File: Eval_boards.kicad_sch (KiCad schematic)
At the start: 0 parts

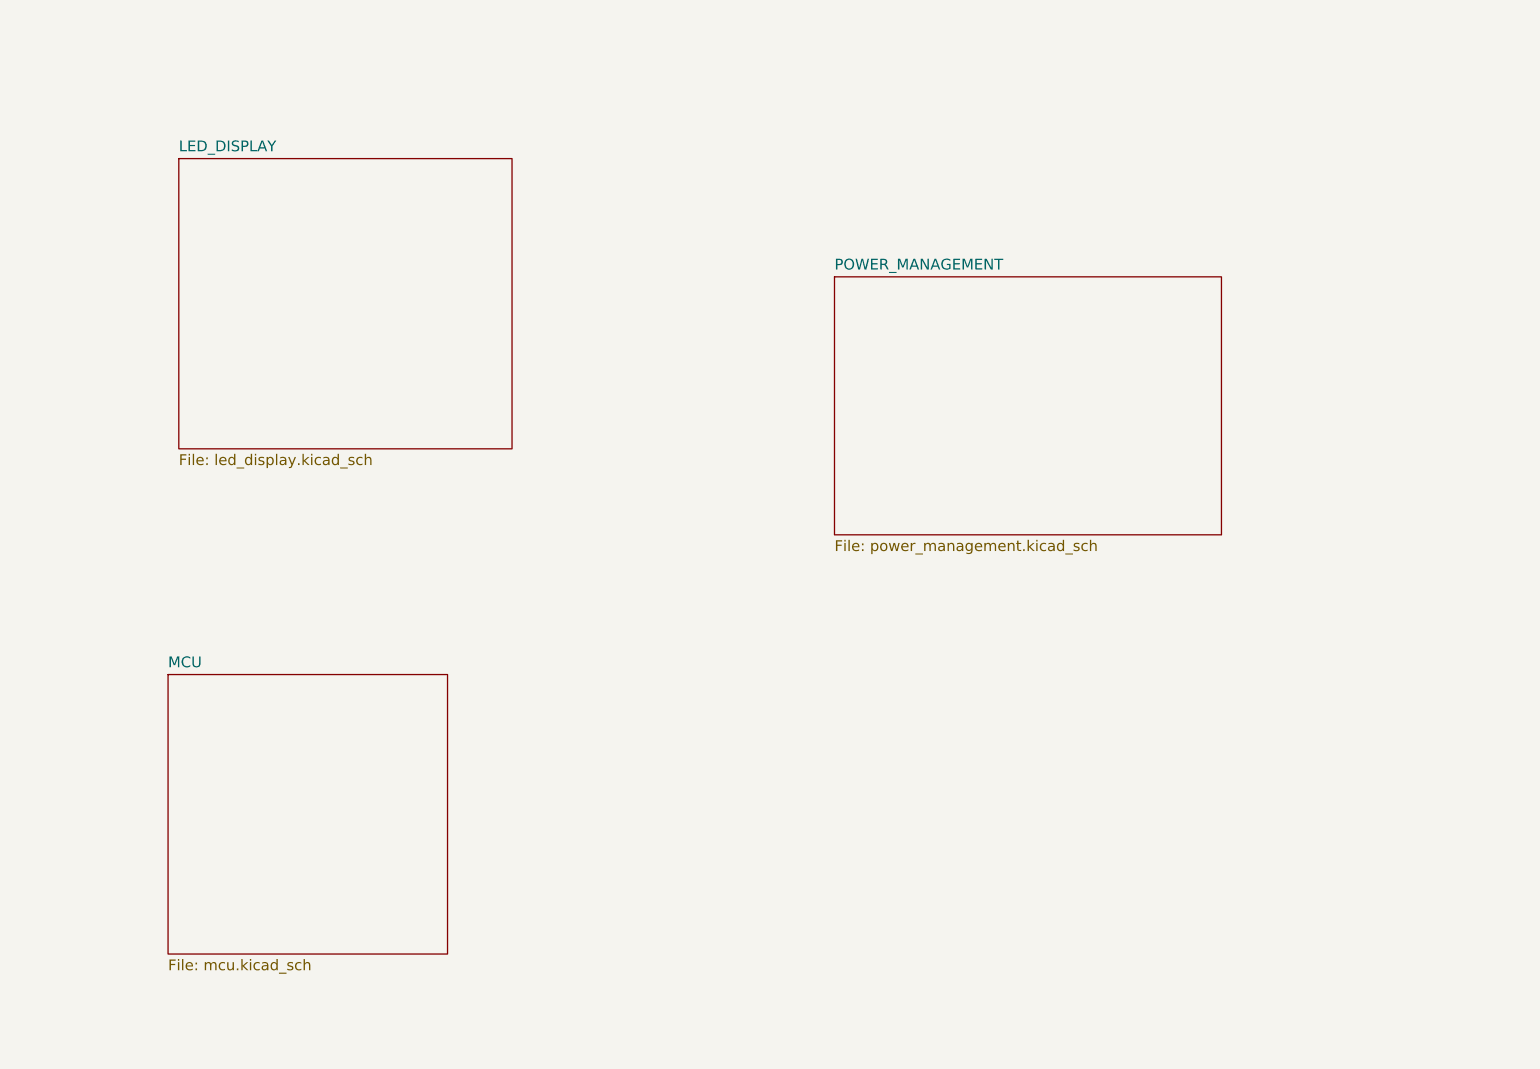
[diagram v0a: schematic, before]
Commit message: Change of concept - one board, not multiple
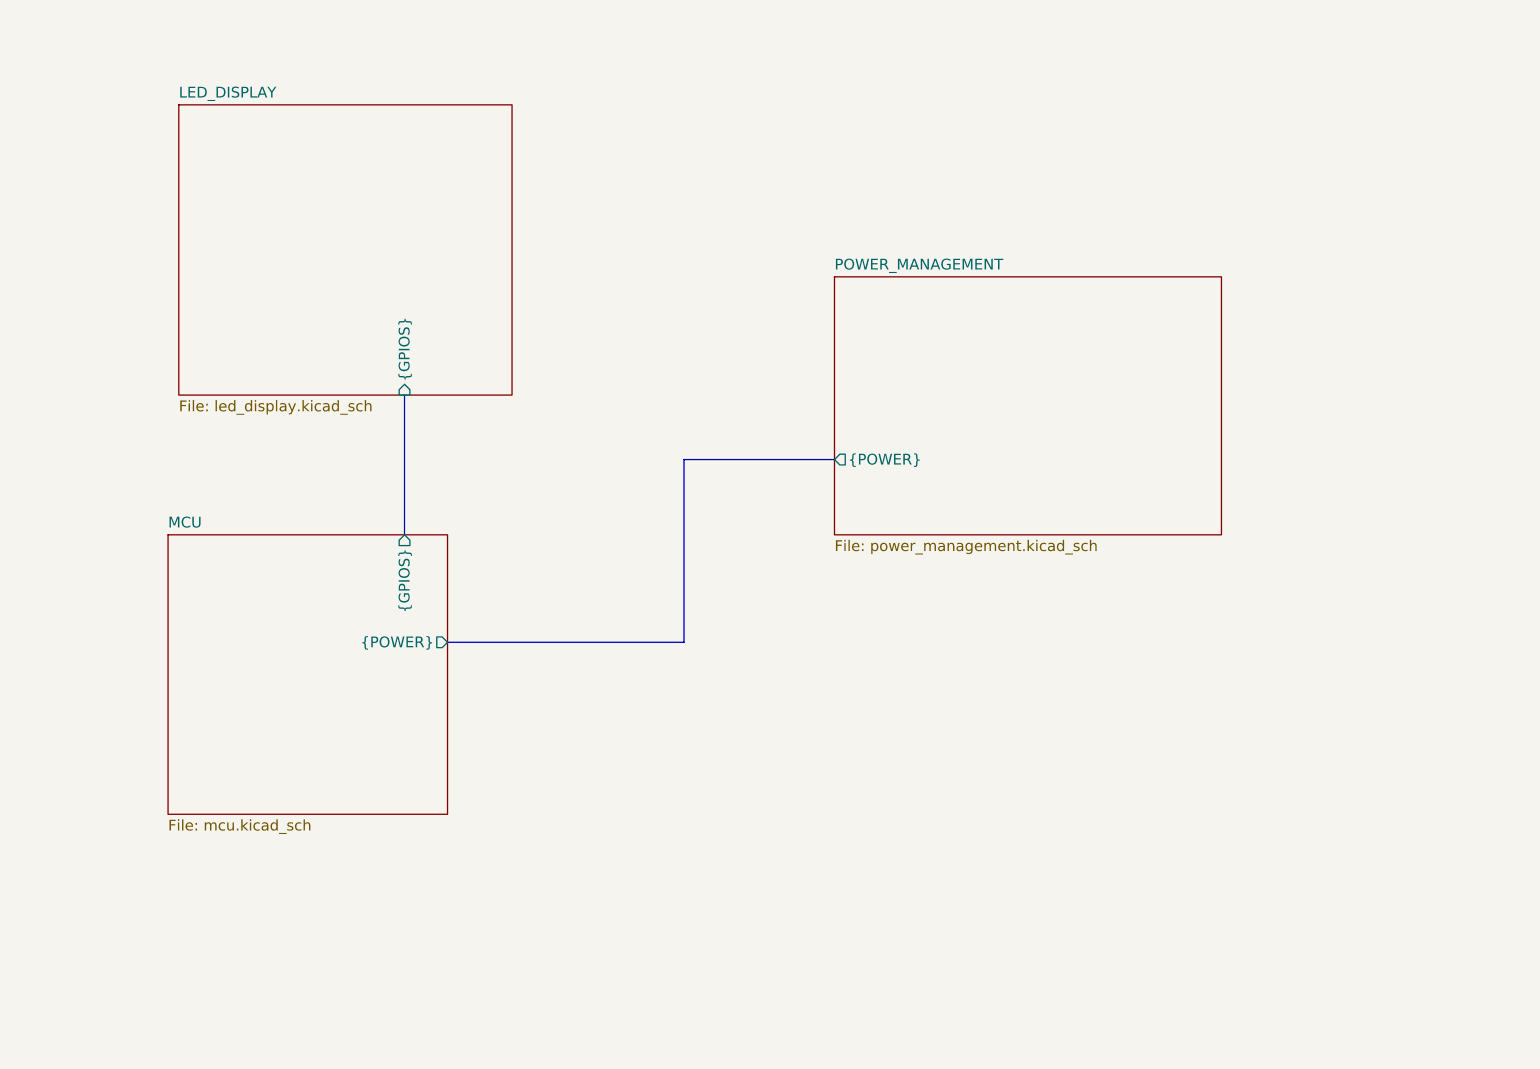
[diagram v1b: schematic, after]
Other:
- sheet LED_DISPLAY ports: added {GPIOS}; removed none
- sheet MCU ports: added {GPIOS}, {POWER}; removed none
- sheet POWER_MANAGEMENT ports: added {POWER}; removed none
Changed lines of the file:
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@@
 		(date "2025-09-10")
 	)
+	(bus
+		(pts
+			(xy 95.25 66.04) (xy 95.25 87.63)
+		)
+		(stroke
+			(width 0)
+			(type default)
+		)
+	)
+	(bus
+		(pts
+			(xy 62.23 58.42) (xy 62.23 74.93)
+		)
+		(stroke
+			(width 0)
+			(type default)
+		)
+	)
+	(bus
+		(pts
+			(xy 95.25 87.63) (xy 67.31 87.63)
+		)
+		(stroke
+			(width 0)
+			(type default)
+		)
+	)
+	(bus
+		(pts
+			(xy 113.03 66.04) (xy 95.25 66.04)
+		)
+		(stroke
+			(width 0)
+			(type default)
+		)
+	)
 	(sheet
-		(at 35.56 30.48)
+		(at 35.56 24.13)
 		(size 39.37 34.29)
 		(exclude_from_sim no)
@@
 		)
 		(property "Sheetname" "LED_DISPLAY"
-			(at 35.56 29.7684 0)
+			(at 35.56 23.4184 0)
 			(effects
 				(font
@@
 		)
 		(property "Sheetfile" "led_display.kicad_sch"
-			(at 35.56 65.3546 0)
+			(at 35.56 59.0046 0)
 			(effects
 				(font
@@
 				)
 				(justify left top)
+			)
+		)
+		(pin "{GPIOS}" input
+			(at 62.23 58.42 270)
+			(effects
+				(font
+					(size 1.27 1.27)
+				)
+				(justify left)
 			)
 		)
@@
 			)
 		)
+		(pin "{POWER}" output
+			(at 113.03 66.04 180)
+			(effects
+				(font
+					(size 1.27 1.27)
+				)
+				(justify left)
+			)
+		)
 		(instances
 			(project "Eval_boards"
@@
 	)
 	(sheet
-		(at 34.29 91.44)
+		(at 34.29 74.93)
 		(size 33.02 33.02)
 		(exclude_from_sim no)
@@
 		)
 		(property "Sheetname" "MCU"
-			(at 34.29 90.7284 0)
+			(at 34.29 74.2184 0)
 			(effects
 				(font
@@
 		)
 		(property "Sheetfile" "mcu.kicad_sch"
-			(at 34.29 125.0446 0)
+			(at 34.29 108.5346 0)
 			(effects
 				(font
@@
 			)
 		)
+		(pin "{GPIOS}" output
+			(at 62.23 74.93 90)
+			(effects
+				(font
+					(size 1.27 1.27)
+				)
+				(justify right)
+			)
+		)
+		(pin "{POWER}" output
+			(at 67.31 87.63 0)
+			(effects
+				(font
+					(size 1.27 1.27)
+				)
+				(justify right)
+			)
+		)

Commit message: Finished pcb project
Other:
- added sheet ACCELEROMETER (accelerometer.kicad_sch)
- sheet MCU ports: added {ACCELEROMETER}; removed none
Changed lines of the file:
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@@
 	(bus
 		(pts
-			(xy 95.25 66.04) (xy 95.25 87.63)
+			(xy 118.11 62.23) (xy 123.19 62.23)
 		)
 		(stroke
@@
 	(bus
 		(pts
-			(xy 62.23 58.42) (xy 62.23 74.93)
+			(xy 62.23 62.23) (xy 67.31 62.23)
 		)
 		(stroke
@@
 	(bus
 		(pts
-			(xy 95.25 87.63) (xy 67.31 87.63)
+			(xy 95.25 48.26) (xy 95.25 54.61)
 		)
 		(stroke
@@
 		)
 	)
-	(bus
-		(pts
-			(xy 113.03 66.04) (xy 95.25 66.04)
-		)
-		(stroke
-			(width 0)
-			(type default)
-		)
-	)
-	(sheet
-		(at 35.56 24.13)
-		(size 39.37 34.29)
+	(sheet
+		(at 123.19 16.51)
+		(size 71.12 83.82)
 		(exclude_from_sim no)
 		(in_bom yes)
@@
 		)
 		(property "Sheetname" "LED_DISPLAY"
-			(at 35.56 23.4184 0)
+			(at 123.19 15.7984 0)
 			(effects
 				(font
@@
 		)
 		(property "Sheetfile" "led_display.kicad_sch"
-			(at 35.56 59.0046 0)
+			(at 123.19 100.9146 0)
 			(effects
 				(font
@@
 		)
 		(pin "{GPIOS}" input
-			(at 62.23 58.42 270)
+			(at 123.19 62.23 180)
 			(effects
 				(font
@@
 	)
 	(sheet
-		(at 113.03 44.45)
-		(size 45.72 30.48)
+		(at 16.51 16.51)
+		(size 45.72 116.84)
 		(exclude_from_sim no)
 		(in_bom yes)
@@
 		)
 		(property "Sheetname" "POWER_MANAGEMENT"
-			(at 113.03 43.7384 0)
+			(at 16.51 15.7984 0)
 			(effects
 				(font
@@
 		)
 		(property "Sheetfile" "power_management.kicad_sch"
-			(at 113.03 75.5146 0)
-			(effects
-				(font
-					(size 1.27 1.27)
-				)
-				(justify left top)
-			)
-		)
-		(pin "{POWER}" output
-			(at 113.03 66.04 180)
-			(effects
-				(font
-					(size 1.27 1.27)
-				)
-				(justify left)
+			(at 16.51 133.9346 0)
+			(effects
+				(font
+					(size 1.27 1.27)
+				)
+				(justify left top)
+			)
+		)
+		(pin "{POWER}" bidirectional
+			(at 62.23 62.23 0)
+			(effects
+				(font
+					(size 1.27 1.27)
+				)
+				(justify right)
 			)
 		)
@@
 	)
 	(sheet
-		(at 34.29 74.93)
-		(size 33.02 33.02)
+		(at 67.31 16.51)
+		(size 50.8 31.75)
+		(exclude_from_sim no)
+		(in_bom yes)
+		(on_board yes)
+		(dnp no)
+		(fields_autoplaced yes)
+		(stroke
+			(width 0.1524)
+			(type solid)
+		)
+		(fill
+			(color 0 0 0 0.0000)
+		)
+		(property "Sheetname" "ACCELEROMETER"
+			(at 67.31 15.7984 0)
+			(effects
+				(font
+					(size 1.27 1.27)
+				)
+				(justify left bottom)
+			)
+		)
+		(property "Sheetfile" "accelerometer.kicad_sch"
+			(at 67.31 48.8446 0)
+			(effects
+				(font
+					(size 1.27 1.27)
+				)
+				(justify left top)
+			)
+		)
+		(pin "{ACCELEROMETER}" bidirectional
+			(at 95.25 48.26 270)
+			(effects
+				(font
+					(size 1.27 1.27)
+				)
+				(justify left)
+			)
+		)
+		(instances
+			(project "Eval_boards"
+				(path "/d7ecb1f3-4916-4ecb-8c6e-b89f175440e1"
+					(page "5")
+				)
+			)
+		)
+	)
+	(sheet
+		(at 67.31 54.61)
+		(size 50.8 45.72)
 		(exclude_from_sim no)
 		(in_bom yes)
@@
 		)
 		(property "Sheetname" "MCU"
-			(at 34.29 74.2184 0)
+			(at 67.31 53.8984 0)
 			(effects
 				(font
@@
 		)
 		(property "Sheetfile" "mcu.kicad_sch"
-			(at 34.29 108.5346 0)
+			(at 67.31 100.9146 0)
 			(effects
 				(font
@@
 		)
 		(pin "{GPIOS}" output
-			(at 62.23 74.93 90)
+			(at 118.11 62.23 0)
 			(effects
 				(font
@@
 			)
 		)
-		(pin "{POWER}" output
-			(at 67.31 87.63 0)
+		(pin "{ACCELEROMETER}" bidirectional
+			(at 95.25 54.61 90)
 			(effects
 				(font
@@
 			)
 		)
+		(pin "{POWER}" bidirectional
+			(at 67.31 62.23 180)
+			(effects
+				(font
+					(size 1.27 1.27)
+				)
+				(justify left)
+			)
+		)
